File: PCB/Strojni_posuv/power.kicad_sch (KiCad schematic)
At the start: 29 parts, among them J2 Button_power_A, J5 POWER, J6 Button_power_B, U4 MIC5365-3.3YC5, U8 TPS62822DLC

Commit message: Starting new Revision 1
addressing some problems and mistakes
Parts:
- C31: footprint Capacitor_SMD:C_0603_1608Metric -> Capacitor_SMD:C_0805_2012Metric
- R12, R17, R18, R44, R45, R46: footprint Resistor_SMD:R_0603_1608Metric -> Resistor_SMD:R_0805_2012Metric
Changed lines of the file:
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@@
 			)
 		)
-		(property "Footprint" "Capacitor_SMD:C_0603_1608Metric"
+		(property "Footprint" "Capacitor_SMD:C_0805_2012Metric"
 			(at 166.0652 44.45 0)
 			(effects
@@
 			)
 		)
-		(property "Footprint" "Resistor_SMD:R_0603_1608Metric"
+		(property "Footprint" "Resistor_SMD:R_0805_2012Metric"
 			(at 119.888 71.12 90)
 			(effects
@@
 			)
 		)
-		(property "Footprint" "Resistor_SMD:R_0603_1608Metric"
+		(property "Footprint" "Resistor_SMD:R_0805_2012Metric"
 			(at 195.58 85.852 90)
 			(effects
@@
 			)
 		)
-		(property "Footprint" "Resistor_SMD:R_0603_1608Metric"
+		(property "Footprint" "Resistor_SMD:R_0805_2012Metric"
 			(at 136.652 44.45 90)
 			(effects
@@
 			)
 		)
-		(property "Footprint" "Resistor_SMD:R_0603_1608Metric"
+		(property "Footprint" "Resistor_SMD:R_0805_2012Metric"
 			(at 221.742 38.1 90)
 			(effects
@@
 			)
 		)
-		(property "Footprint" "Resistor_SMD:R_0603_1608Metric"
+		(property "Footprint" "Resistor_SMD:R_0805_2012Metric"
 			(at 221.742 50.8 90)
 			(effects
@@
 			)
 		)
-		(property "Footprint" "Resistor_SMD:R_0603_1608Metric"
+		(property "Footprint" "Resistor_SMD:R_0805_2012Metric"
 			(at 122.428 83.82 90)
 			(effects

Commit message: Resolving problems from list
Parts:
- added SW6: Emergency_stop, Emergency:Emergency_stop, symbol Switch:SW_Push_Open
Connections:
- net GND: now also SW6.2 (B); no longer J6.1 (Pin_1)
- new net: J6.1 (Pin_1), SW6.1 (A)
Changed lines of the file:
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@@
 	(wire
 		(pts
+			(xy 77.47 106.68) (xy 88.9 106.68)
+		)
+		(stroke
+			(width 0)
+			(type default)
+		)
+	)
+	(wire
+		(pts
 			(xy 118.11 172.085) (xy 118.11 172.72)
 		)
@@
 	(polyline
 		(pts
-			(xy 71.12 95.25) (xy 71.12 129.54)
+			(xy 101.6 95.25) (xy 101.6 129.54)
 		)
 		(stroke
@@
 	(wire
 		(pts
-			(xy 53.34 106.68) (xy 58.42 106.68)
+			(xy 53.34 106.68) (xy 67.31 106.68)
 		)
 		(stroke
@@
 	(polyline
 		(pts
-			(xy 21.59 129.54) (xy 71.12 129.54)
+			(xy 21.59 129.54) (xy 101.6 129.54)
 		)
 		(stroke
@@
 		(lib_name "GND_1")
 		(lib_id "power:GND")
-		(at 58.42 106.68 90)
+		(at 88.9 106.68 90)
 		(unit 1)
 		(exclude_from_sim no)
@@
 		(fields_autoplaced yes)
 		(property "Reference" "#PWR085"
-			(at 64.77 106.68 0)
+			(at 95.25 106.68 0)
 			(effects
 				(font
@@
 		)
 		(property "Value" "GND"
-			(at 62.23 106.6799 90)
+			(at 92.71 106.6799 90)
 			(effects
 				(font
@@
 		)
 		(property "Footprint" ""
-			(at 58.42 106.68 0)
+			(at 88.9 106.68 0)
 			(effects
 				(font
@@
 		)
 		(property "Datasheet" ""
-			(at 58.42 106.68 0)
+			(at 88.9 106.68 0)
 			(effects
 				(font
@@
 		)
 		(property "Description" "Power symbol creates a global label with name \"GND\" , ground"
-			(at 58.42 106.68 0)
+			(at 88.9 106.68 0)
 			(effects
 				(font
@@
 					(unit 1)
 				)
+			)
+		)
+	)
+	(symbol
+		(lib_id "Switch:SW_Push_Open")
+		(at 72.39 106.68 0)
+		(unit 1)
+		(exclude_from_sim no)
+		(in_bom yes)
+		(on_board yes)
+		(dnp no)
+		(fields_autoplaced yes)
+		(property "Reference" "SW6"
+			(at 72.39 100.33 0)
+			(effects
+				(font
+					(size 1.27 1.27)
+				)
+			)
+		)
+		(property "Value" "Emergency_stop"
+			(at 72.39 102.87 0)
+			(effects
+				(font
+					(size 1.27 1.27)
+				)
+			)
+		)
+		(property "Footprint" "Emergency:Emergency_stop"
+			(at 72.39 101.6 0)
+			(effects
+				(font
+					(size 1.27 1.27)
+				)
+				(hide yes)
+			)
+		)
+		(property "Datasheet" "~"
+			(at 72.39 101.6 0)
+			(effects
+				(font
+					(size 1.27 1.27)
+				)
+				(hide yes)
+			)
+		)
+		(property "Description" "Push button switch, push-to-open, generic, two pins"
+			(at 72.39 106.68 0)
+			(effects
+				(font
+					(size 1.27 1.27)
+				)
+				(hide yes)
+			)
+		)
+		(pin "2"
+		)
+		(pin "1"
+		)
+		(instances
+			(project ""
+				(path "/36664f97-4753-4126-9e35-a8ab7ac5ffb4/ee0b1210-eaee-41ba-b593-299cdfd1f985"
+					(reference "SW6")
+					(unit 1)
+				)

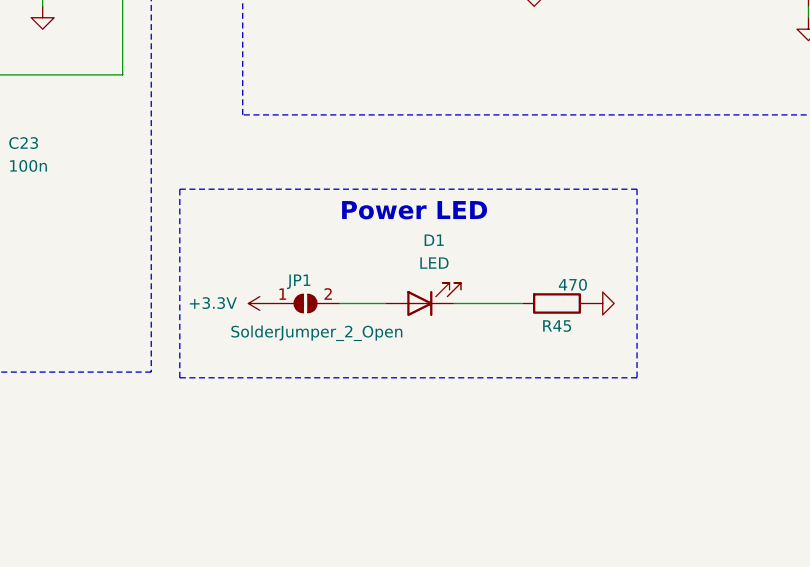
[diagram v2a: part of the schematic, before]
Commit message: PCB done?
I did all the routing and component placement on PCB
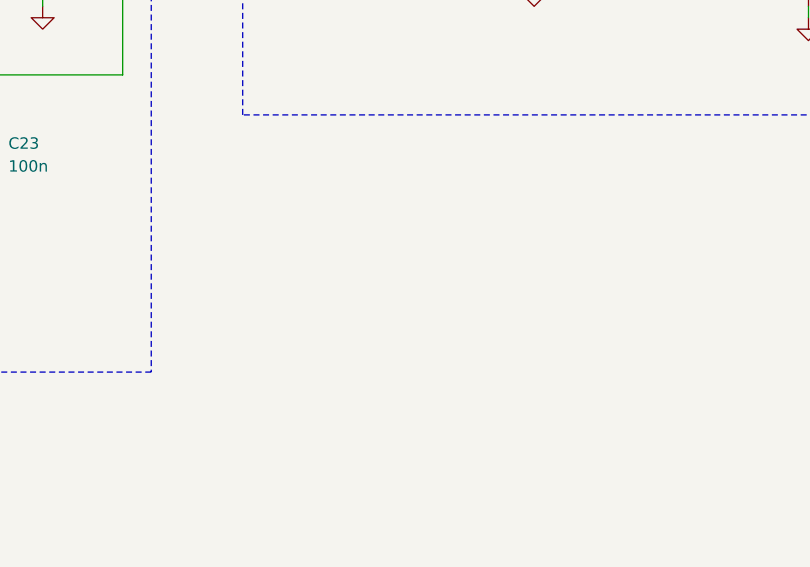
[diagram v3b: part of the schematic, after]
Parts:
- removed D1: LED, LED_SMD:LED_0603_1608Metric, symbol Device:LED
- removed JP1: SolderJumper_2_Open, Jumper:SolderJumper-2_P1.3mm_Open_TrianglePad1.0x1.5mm, symbol Jumper:SolderJumper_2_Open
- removed R45: 470, Resistor_SMD:R_0805_2012Metric, symbol Device:R
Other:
- note removed: "Power LED"
